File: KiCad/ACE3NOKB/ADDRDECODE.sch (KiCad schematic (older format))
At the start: 11 parts

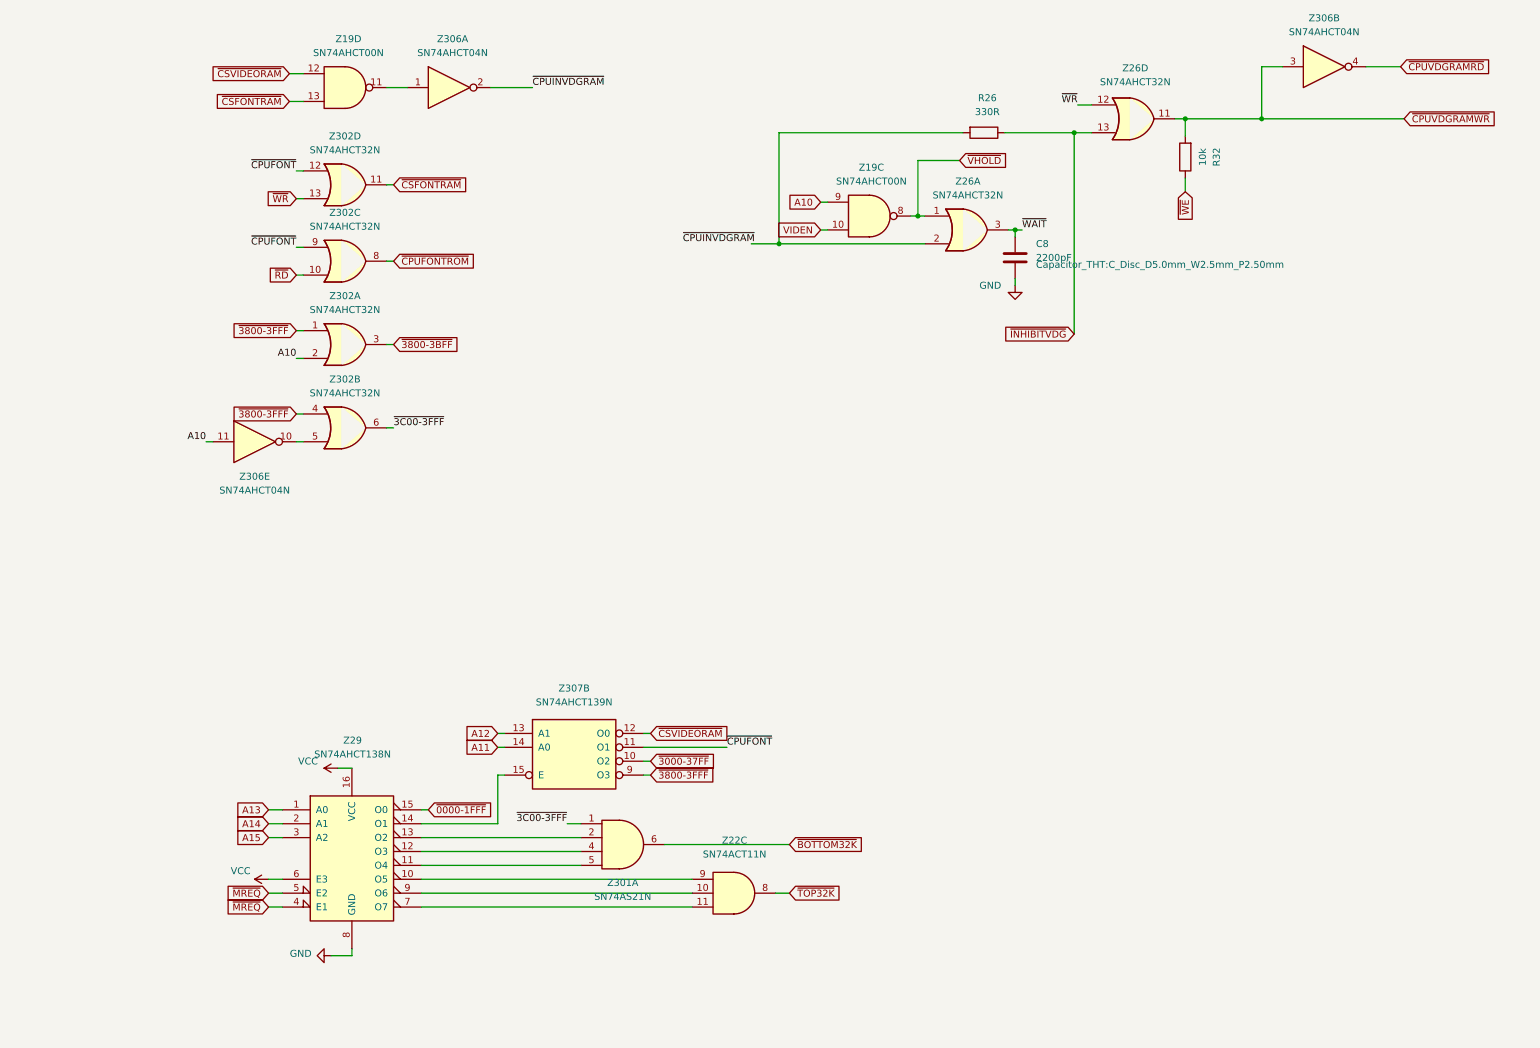
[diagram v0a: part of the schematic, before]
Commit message: Update ACE3NOKB to reflect errors in Mem Decode. ACE5NOKB test SMT ideas. Added 180 & 380.
Signed-off-by: John Bradley <flypie@rocketmail.com>
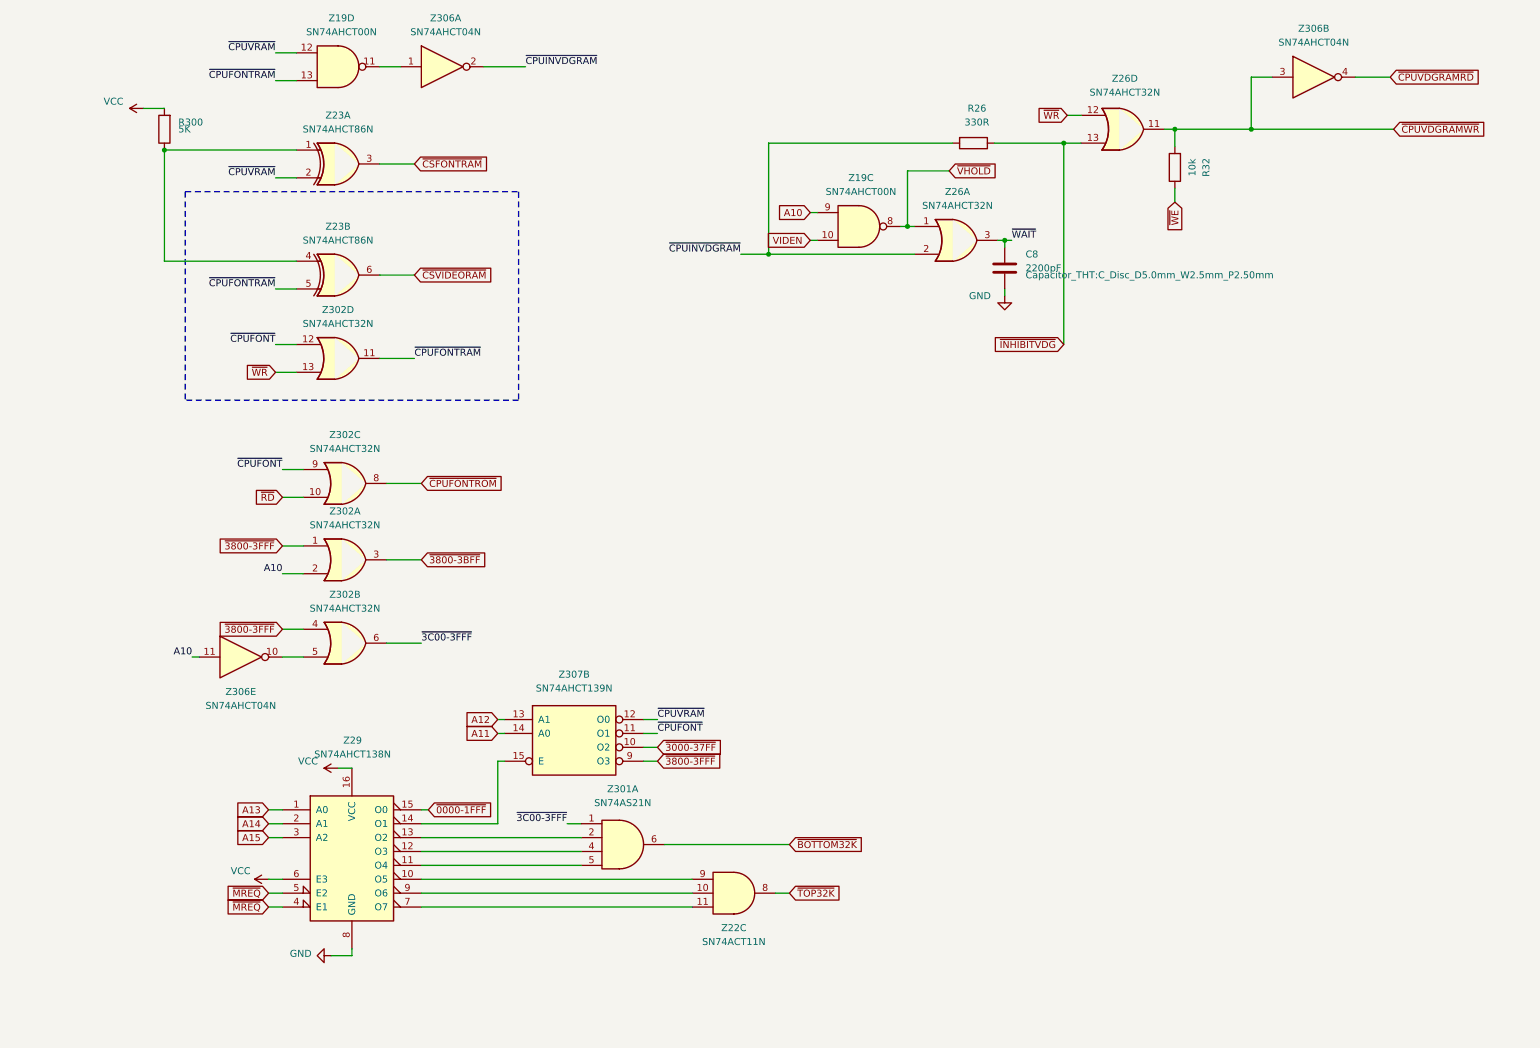
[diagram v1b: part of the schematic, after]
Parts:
- added R300: 5K, Resistor_THT:R_Axial_DIN0204_L3.6mm_D1.6mm_P1.90mm_Vertical, symbol Device:R
- added Z23: SN74AHCT86N, Package_DIP:DIP-14_W7.62mm, symbol 74xx:74LS86
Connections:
- net VCC: now also R300.2
- net ~CSFONTRAM: now also Z23.3; no longer Z19.13, Z302.11
- net ~CSVIDEORAM: now also Z23.6; no longer Z19.12, Z307.12 (O0)
- new net: R300.1, Z23.1, Z23.4
- new net ~CPUFONTRAM: Z19.13, Z23.5, Z302.11
- new net ~CPUVRAM: Z19.12, Z23.2, Z307.12 (O0)
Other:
- moved on the sheet: C8, R26, R32, Z19C, Z19D, Z26A, Z26D, Z302A, Z302B, Z302C, Z306A, Z306B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

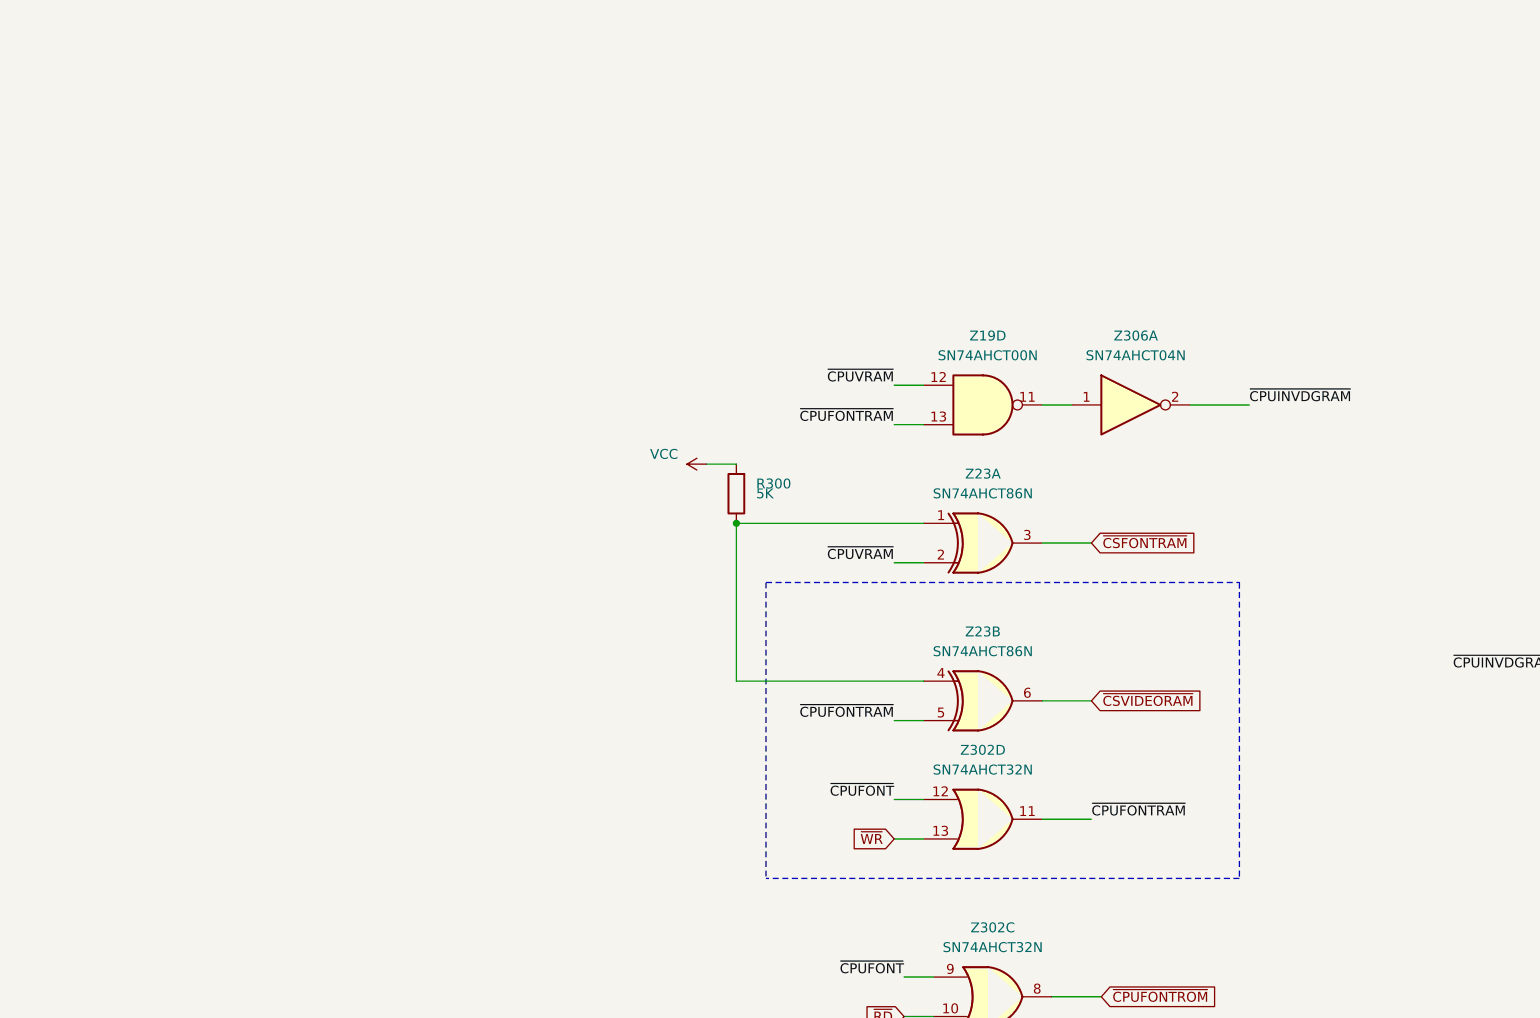
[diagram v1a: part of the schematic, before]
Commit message: Fix several problems with Chip Select. Reconnect the Data bus for the VDG to the CPU bus which has become disconnected.
Signed-off-by: John Bradley <flypie@rocketmail.com>
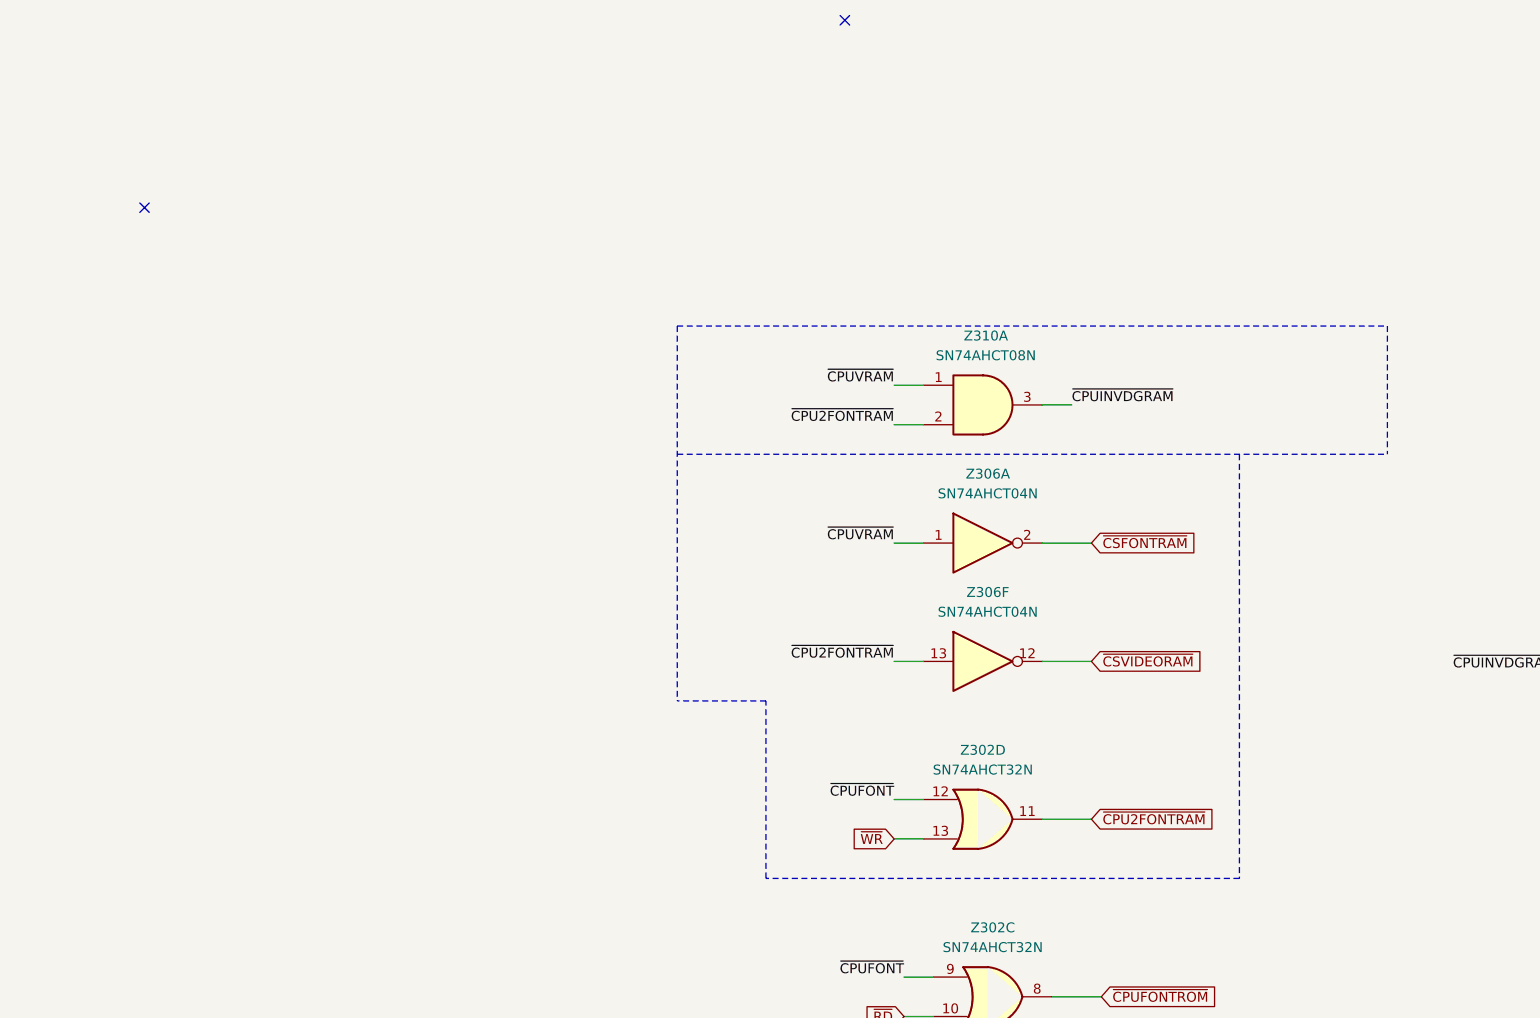
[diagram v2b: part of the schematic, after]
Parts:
- removed R300: 5K, Resistor_THT:R_Axial_DIN0204_L3.6mm_D1.6mm_P1.90mm_Vertical, symbol Device:R
- removed unit 4 of Z19
- removed Z23: SN74AHCT86N, Package_DIP:DIP-14_W7.62mm, symbol 74xx:74LS86
- added unit 6 of Z306
- added Z310: SN74AHCT08N, Package_DIP:DIP-14_W7.62mm, symbol 74xx:74LS08
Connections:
- net ~CPUINVDGRAM: now also Z310.3; no longer Z306.2
- net ~CPUVRAM: now also Z306.1, Z310.1
- net ~CSFONTRAM: now also Z306.2
- net ~CSVIDEORAM: now also Z306.12
- net ~CPUFONTRAM renamed ~CPU2FONTRAM
- net ~CPU2FONTRAM: now also Z306.13, Z310.2
- no-connect marks 1 -> 3
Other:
- moved on the sheet: Z306A
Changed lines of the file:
@@
 Text Label 1750 4550 2    50   ~ 0
 A10
-Text Label 3500 900  0    50   ~ 0
+Text Label 2600 900  0    50   ~ 0
 ~CPUINVDGRAM
-Wire Wire Line
-	3200 900  3500 900
 Wire Wire Line
 	6875 1450 7375 1450
@@
 Wire Wire Line
 	3800 6350 3900 6350
-Text GLabel 2700 2400 2    50   Input ~ 0
+Text GLabel 2700 2200 2    50   Input ~ 0
 ~CSVIDEORAM
 Text GLabel 1750 4950 0    50   Input ~ 0
@@
 ~CPUFONT
 $Comp
-L 74xx:74LS00 Z19
-U 4 1 631ECF0D
-P 2150 900
-F 0 "Z19" H 2175 1250 50  0000 C CNN
-F 1 "SN74AHCT00N" H 2175 1150 50  0000 C CNN
-F 2 "Package_DIP:DIP-14_W7.62mm" H 2150 900 50  0001 C CNN
-F 3 "http://www.ti.com/lit/gpn/sn74ls00" H 2150 900 50  0001 C CNN
-F 4 "SN74AHCT00N" H 2150 900 50  0001 C CNN "Manufacturer_Part_Number"
-F 5 "Texas Instruments" H 2150 900 50  0001 C CNN "Manufacturer_Name"
-	4    2150 900
-	1    0    0    -1
-$EndComp
-$Comp
 L 74xx:74LS04 Z306
 U 1 1 631F47D3
-P 2900 900
-F 0 "Z306" H 2925 1250 50  0000 C CNN
-F 1 "SN74AHCT04N" H 2925 1150 50  0000 C CNN
-F 2 "Package_DIP:DIP-14_W7.62mm" H 2900 900 50  0001 C CNN
-F 3 "http://www.ti.com/lit/gpn/snSN74AHCT04" H 2900 900 50  0001 C CNN
-F 4 "SN74AHCT04N" H 2900 900 50  0001 C CNN "Manufacturer_Part_Number"
-F 5 "Texas Instruments" H 2900 900 50  0001 C CNN "Manufacturer_Name"
-	1    2900 900
-	1    0    0    -1
-$EndComp
-Wire Wire Line
-	2600 900  2450 900
-$Comp
-L 74xx:74LS86 Z23
-U 1 1 602A84E8
 P 2150 1600
-F 0 "Z23" H 2150 1950 50  0000 C CNN
-F 1 "SN74AHCT86N" H 2150 1850 50  0000 C CNN
+F 0 "Z306" H 2175 1950 50  0000 C CNN
+F 1 "SN74AHCT04N" H 2175 1850 50  0000 C CNN
 F 2 "Package_DIP:DIP-14_W7.62mm" H 2150 1600 50  0001 C CNN
-F 3 "74xx/74ls86.pdf" H 2150 1600 50  0001 C CNN
-F 4 "SN74AHCT86N" H 2150 1600 50  0001 C CNN "Manufacturer_Part_Number"
+F 3 "http://www.ti.com/lit/gpn/snSN74AHCT04" H 2150 1600 50  0001 C CNN
+F 4 "SN74AHCT04N" H 2150 1600 50  0001 C CNN "Manufacturer_Part_Number"
 F 5 "Texas Instruments" H 2150 1600 50  0001 C CNN "Manufacturer_Name"
 	1    2150 1600
@@
 $EndComp
 Wire Wire Line
+	2600 900  2450 900
+Wire Wire Line
 	4350 5600 4450 5600
 Wire Wire Line
 	2450 1600 2700 1600
-$Comp
-L Device:R R300
-U 1 1 6032E0C4
-P 900 1350
-F 0 "R300" H 800 1300 50  0000 R CNN
-F 1 "5K" H 800 1350 50  0000 R CNN
-F 2 "Resistor_THT:R_Axial_DIN0204_L3.6mm_D1.6mm_P1.90mm_Vertical" V 830 1350 50  0001 C CNN
-F 3 "" H 900 1350 50  0001 C CNN
-F 4 "Vishay" H 900 1350 50  0001 C CNN "Manufacturer_Name"
-F 5 "MBA02040C1002FRP00 " H 900 1350 50  0001 C CNN "Manufacturer_Part_Number"
-	1    900  1350
-	-1   0    0    1
-$EndComp
-Wire Wire Line
-	1850 1500 900  1500
-Wire Wire Line
-	900  1200 750  1200
-$Comp
-L power:VCC #~PWR0116
-U 1 1 6032E0CC
-P 750 1200
-F 0 "#~PWR0116" H 750 1050 50  0001 C CNN
-F 1 "VCC" V 800 1345 50  0000 L CNN
-F 2 "" H 750 1200 50  0001 C CNN
-F 3 "" H 750 1200 50  0001 C CNN
-	1    750  1200
-	0    -1   -1   0
-$EndComp
-Wire Wire Line
-	1850 1700 1700 1700
+Wire Wire Line
+	1850 1600 1700 1600
 Text Label 4450 5600 0    50   ~ 0
 ~CPUVRAM
-Text Label 1700 1700 2    50   ~ 0
+Text Label 1700 1600 2    50   ~ 0
 ~CPUVRAM
-$Comp
-L 74xx:74LS86 Z23
-U 2 1 6034DB6A
-P 2150 2400
-F 0 "Z23" H 2150 2750 50  0000 C CNN
-F 1 "SN74AHCT86N" H 2150 2650 50  0000 C CNN
-F 2 "Package_DIP:DIP-14_W7.62mm" H 2150 2400 50  0001 C CNN
-F 3 "74xx/74ls86.pdf" H 2150 2400 50  0001 C CNN
-F 4 "SN74AHCT86N" H 2150 2400 50  0001 C CNN "Manufacturer_Part_Number"
-F 5 "Texas Instruments" H 2150 2400 50  0001 C CNN "Manufacturer_Name"
-	2    2150 2400
-	1    0    0    -1
-$EndComp
-Wire Wire Line
-	2450 2400 2700 2400
-Wire Wire Line
-	1850 2500 1700 2500
-Wire Notes Line
-	1050 1800 3450 1800
+Wire Wire Line
+	2450 2200 2700 2200
+Wire Wire Line
+	1850 2200 1700 2200
 Text GLabel 7400 1250 0    50   Input ~ 0
 ~WR
-Wire Wire Line
-	900  2300 900  1500
-Wire Wire Line
-	900  2300 1850 2300
-Connection ~ 900  1500
+Text Label 1700 2200 2    50   ~ 0
+~CPU2FONTRAM
+Text Label 1700 1000 2    50   ~ 0
+~CPU2FONTRAM
+Text Label 1700 800  2    50   ~ 0
+~CPUVRAM
+Wire Notes Line
+	1050 2400 600  2400
+Wire Notes Line
+	1050 3300 1050 2400
+Wire Notes Line
+	3450 1150 3450 3300
+Wire Notes Line
+	3450 3300 1050 3300
+Text GLabel 1700 3100 0    50   Input ~ 0
+~WR
+Wire Wire Line
+	2450 3000 2700 3000
+Wire Wire Line
+	1850 2900 1700 2900
+Text Label 1700 2900 2    50   ~ 0
+~CPUFONT
+Wire Wire Line
+	1850 3100 1700 3100
 $Comp
 L 74xx:74LS32 Z302
@@
 	1    0    0    -1
 $EndComp
-Wire Wire Line
-	1850 3100 1700 3100
-Text Label 1700 2900 2    50   ~ 0
-~CPUFONT
-Wire Wire Line
-	1850 2900 1700 2900
-Wire Wire Line
-	2450 3000 2700 3000
-Text GLabel 1700 3100 0    50   Input ~ 0
-~WR
-Text Label 2700 3000 0    50   ~ 0
-~CPUFONTRAM
-Text Label 1700 2500 2    50   ~ 0
-~CPUFONTRAM
-Wire Notes Line
-	3450 3300 1050 3300
-Wire Notes Line
-	3450 1800 3450 3300
-Wire Notes Line
-	1050 1800 1050 3300
-Text Label 1700 1000 2    50   ~ 0
-~CPUFONTRAM
-Text Label 1700 800  2    50   ~ 0
-~CPUVRAM
+Wire Notes Line
+	600  500  4200 500
+Wire Notes Line
+	4200 500  4200 1150
+Wire Notes Line
+	600  500  600  2400
+Wire Notes Line
+	600  1150 4200 1150
+Text GLabel 2700 3000 2    50   Input ~ 0
+~CPU2FONTRAM
+$Comp
+L 74xx:74LS08 Z310
+U 1 1 617C56C3
+P 2150 900
+F 0 "Z310" H 2165 1250 50  0000 C CNN
+F 1 "SN74AHCT08N" H 2165 1150 50  0000 C CNN
+F 2 "Package_DIP:DIP-14_W7.62mm" H 2150 900 50  0001 C CNN
+F 3 "http://www.ti.com/lit/gpn/sn74ls00" H 2150 900 50  0001 C CNN
+F 4 "74xx:74LS08" H 2150 900 50  0001 C CNN "Manufacturer_Part_Number"
+F 5 "Texas Instruments" H 2150 900 50  0001 C CNN "Manufacturer_Name"
+	1    2150 900
+	1    0    0    -1
+$EndComp
+NoConn ~ 1450 -1050
+NoConn ~ -2100 -100
+$Comp
+L 74xx:74LS04 Z306
+U 6 1 618F659B
+P 2150 2200
+F 0 "Z306" H 2175 2550 50  0000 C CNN
+F 1 "SN74AHCT04N" H 2175 2450 50  0000 C CNN
+F 2 "Package_DIP:DIP-14_W7.62mm" H 2150 2200 50  0001 C CNN
+F 3 "http://www.ti.com/lit/gpn/snSN74AHCT04" H 2150 2200 50  0001 C CNN
+F 4 "SN74AHCT04N" H 2150 2200 50  0001 C CNN "Manufacturer_Part_Number"
+F 5 "Texas Instruments" H 2150 2200 50  0001 C CNN "Manufacturer_Name"
+	6    2150 2200
+	1    0    0    -1
+$EndComp
 $EndSCHEMATC
